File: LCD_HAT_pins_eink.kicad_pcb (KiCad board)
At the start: 4 copper layers, 45.7 x 80.4 mm, 32 parts, among them J1 Qwiic, J2 LCD, J3 PWR_JUMPER, J5 AFC24-S24FIC-00, Q1 Si1308, SW1 SW_Push, SW2 SW_Push, U1 SeeeduinoXIAO

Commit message: FAB Files 1.0
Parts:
- removed J3: PWR_JUMPER, Connector_PinHeader_2.54mm:PinHeader_1x02_P2.54mm_Vertical
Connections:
- J2 pad 2: Net-(J2-Pin_2) -> +3.3V
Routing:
- net Net-(J2-Pin_2): track 8.72 -> 0.00 mm

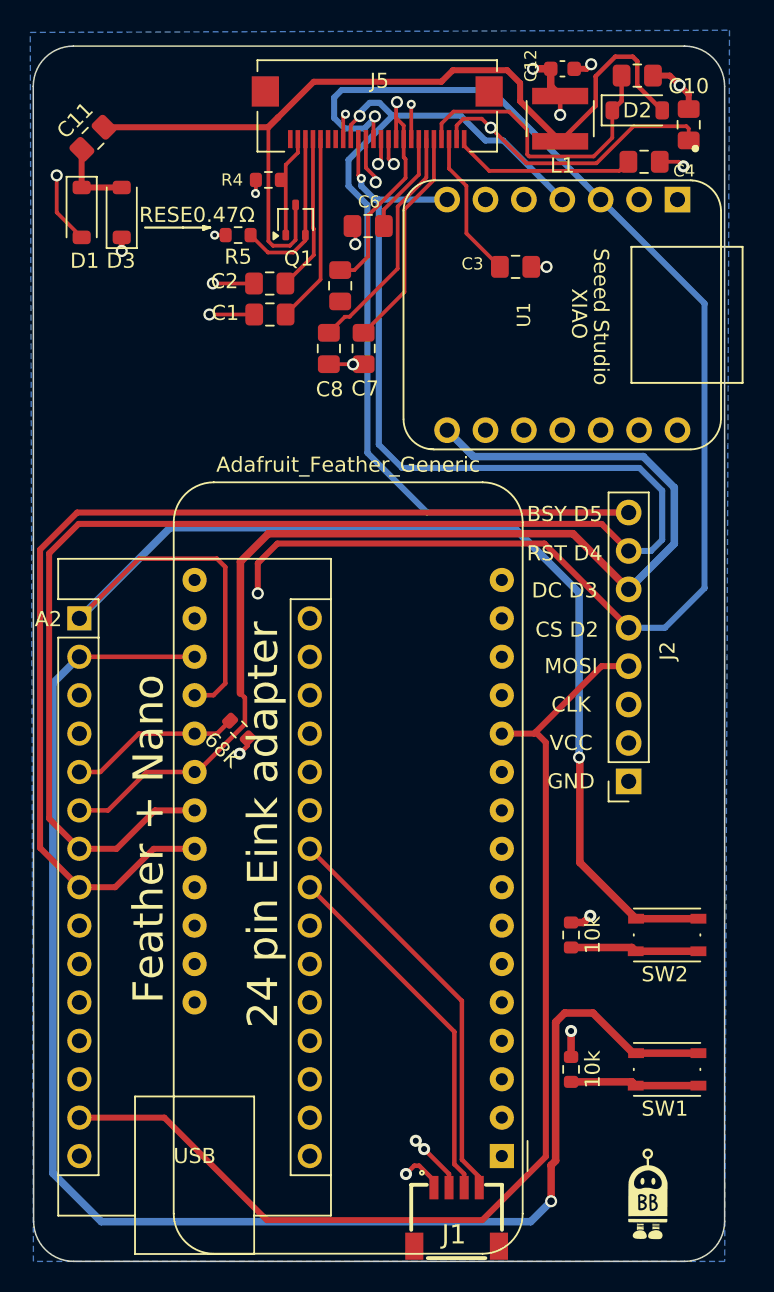
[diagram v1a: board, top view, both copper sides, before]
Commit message: FIX pin not connected to GND in 24 pin FPC
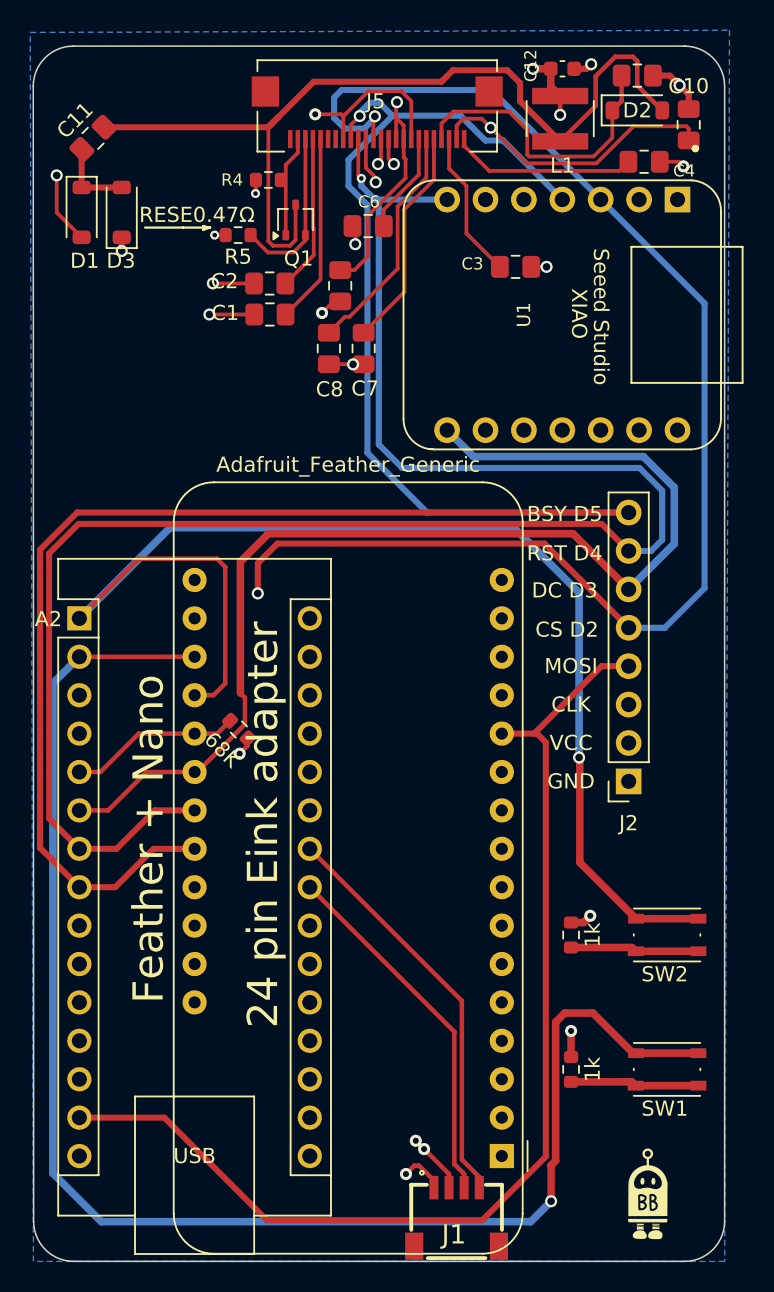
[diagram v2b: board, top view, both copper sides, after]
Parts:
- J5: value AFC24-S24FIC-00 -> CONN_AFC24-S24FIC-00_JUS
- R1, R2: value 10k -> 1k
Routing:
- net GND: track 29.9 -> 38.3 mm
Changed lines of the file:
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@@
 		(sheetname "/")
 		(sheetfile "LCD_HAT_pins_eink.kicad_sch")
-		(attr through_hole exclude_from_bom)
+		(attr through_hole exclude_from_pos_files exclude_from_bom)
 		(fp_line
 			(start -1.4 -3.94)
@@
 			)
 		)
-		(property "Value" "10k"
+		(property "Value" "1k"
 			(at 0 1.43 90)
 			(layer "F.SilkS")
@@
 		(at 134.5 42.954399 180)
 		(property "Reference" "J5"
-			(at -0.15 1.654399 0)
+			(at 0.1 0.304399 0)
 			(layer "F.SilkS")
 			(effects
@@
 			)
 		)
-		(property "Value" "AFC24-S24FIC-00"
-			(at 0.49 4 0)
+		(property "Value" "CONN_AFC24-S24FIC-00_JUS"
+			(at 0.49 4 180)
 			(layer "F.SilkS")
 			(hide yes)
@@
 		)
 		(property "Datasheet" ""
-			(at 0 0 0)
+			(at 0 0 180)
 			(layer "F.Fab")
 			(hide yes)
@@
 		)
 		(property "Description" ""
-			(at 0 0 0)
-			(layer "F.Fab")
-			(hide yes)
-			(effects
-				(font
-					(size 1.27 1.27)
-					(thickness 0.15)
-				)
-			)
-		)
-		(property "LCSC" "C262292"
 			(at 0 0 180)
-			(unlocked yes)
 			(layer "F.Fab")
 			(hide yes)
 			(effects
 				(font
-					(size 1 1)
+					(size 1.27 1.27)
 					(thickness 0.15)
 				)
@@
 		(sheetname "/")
 		(sheetfile "LCD_HAT_pins_eink.kicad_sch")
-		(attr through_hole)
+		(attr smd)
 		(fp_line
 			(start 7.9248 3.022599)
@@
 		)
 		(fp_text user "*"
-			(at 0 0 0)
+			(at 0 0 180)
 			(layer "F.SilkS")
 			(hide yes)
@@
 		)
 		(fp_text user "Copyright 2021 Accelerated Designs. All rights reserved."
-			(at 0 0 0)
+			(at 0 0 180)
 			(layer "Cmts.User")
 			(effects
@@
 		)
 		(fp_text user "*"
-			(at 0 0 0)
+			(at 0 0 180)
 			(layer "F.Fab")
 			(effects
@@
 		(sheetname "/")
 		(sheetfile "LCD_HAT_pins_eink.kicad_sch")
-		(attr through_hole exclude_from_bom)
+		(attr through_hole exclude_from_pos_files exclude_from_bom)
 		(fp_line
 			(start 21.7 -3.81)
@@
 		(sheetname "/")
 		(sheetfile "LCD_HAT_pins_eink.kicad_sch")
-		(attr through_hole)
+		(attr smd)
 		(fp_line
 			(start 1.17475 -2.2225)
@@
 			)
 		)
-		(property "Value" "10k"
+		(property "Value" "1k"
 			(at 0 1.43 90)
 			(layer "F.SilkS")
@@
 			)
 		)
-		(property "LCSC" "C25804"
+		(property "LCSC" "C11702"
 			(at 0 0 90)
 			(unlocked yes)
@@
 		(tags "Through hole socket strip THT 1x08 2.54mm single row")
 		(property "Reference" "J2"
-			(at -2.57 8.63 90)
+			(at 0 -2.77 180)
 			(layer "F.SilkS")
 			(effects
@@
 		)
 		(property "Value" "LCD"
-			(at 0 20.55 0)
+			(at 0 20.55 180)
 			(layer "F.Fab")
 			(effects
@@
 		(sheetname "/")
 		(sheetfile "LCD_HAT_pins_eink.kicad_sch")
-		(attr through_hole)
+		(attr through_hole exclude_from_pos_files exclude_from_bom)
 		(fp_line
 			(start 1.33 1.27)
@@
 		)
 		(fp_text user "${REFERENCE}"
-			(at 0 8.89 90)
+			(at 0 8.89 270)
 			(layer "F.Fab")
 			(effects
@@
 			(pintype "passive")
 		)
-		(pad "2" thru_hole oval
+		(pad "2" thru_hole circle
 			(at 0 2.54 180)
 			(size 1.7 1.7)
@@
 			(pintype "passive")
 		)
-		(pad "3" thru_hole oval
+		(pad "3" thru_hole circle
 			(at 0 5.08 180)
 			(size 1.7 1.7)
@@
 			(pintype "passive")
 		)
-		(pad "4" thru_hole oval
+		(pad "4" thru_hole circle
 			(at 0 7.62 180)
 			(size 1.7 1.7)
@@
 			(pintype "passive")
 		)
-		(pad "5" thru_hole oval
+		(pad "5" thru_hole circle
 			(at 0 10.16 180)
 			(size 1.7 1.7)
@@
 			(pintype "passive")
 		)
-		(pad "6" thru_hole oval
+		(pad "6" thru_hole circle
 			(at 0 12.7 180)
 			(size 1.7 1.7)
@@
 			(pintype "passive")
 		)
-		(pad "7" thru_hole oval
+		(pad "7" thru_hole circle
 			(at 0 15.24 180)
 			(size 1.7 1.7)
@@
 			(pintype "passive")
 		)
-		(pad "8" thru_hole oval
+		(pad "8" thru_hole circle
 			(at 0 17.78 180)
 			(size 1.7 1.7)
@@
 		)
 		(embedded_fonts no)
-		(model "${KICAD6_3DMODEL_DIR}/Connector_PinSocket_2.54mm.3dshapes/PinSocket_1x08_P2.54mm_Vertical.wrl"
+		(model "${KICAD9_3DMODEL_DIR}/Connector_PinSocket_2.54mm.3dshapes/PinSocket_1x08_P2.54mm_Vertical.step"
 			(offset
 				(xyz 0 0 0)
@@
 		(sheetname "/")
 		(sheetfile "LCD_HAT_pins_eink.kicad_sch")
-		(attr smd exclude_from_bom)
+		(attr through_hole exclude_from_pos_files exclude_from_bom)
 		(fp_line
 			(start -6.9 10.5)
@@
 	)
 	(segment
+		(start 130.4 43.51)
+		(end 132.109998 43.51)
+		(width 0.25)
+		(layer "F.Cu")
+		(net 45)
+	)
+	(segment
 		(start 126.475 48.725)
 		(end 126.45 48.75)
@@
 	)
 	(segment
+		(start 136.750001 42.631313)
+		(end 136.102562 41.983874)
+		(width 0.25)
+		(layer "F.Cu")
+		(net 45)
+	)
+	(segment
+		(start 136.750001 45.149999)
+		(end 136.750001 42.631313)
+		(width 0.25)
+		(layer "F.Cu")
+		(net 45)
+	)
+	(segment
+		(start 136.102562 41.983874)
+		(end 133.916126 41.983874)
+		(width 0.25)
+		(layer "F.Cu")
+		(net 45)
+	)
+	(segment
 		(start 132.7875 60.0375)
 		(end 132.8 60.05)
@@
 	)
 	(segment
-		(start 136.750001 45.149999)
-		(end 136.75 42.85)
-		(width 0.25)
-		(layer "F.Cu")
-		(net 45)
-	)
-	(segment
 		(start 147.32 105.855)
 		(end 147.32 104.14)
@@
 	)
 	(segment
+		(start 130.41 43.5)
+		(end 130.4 43.51)
+		(width 0.25)
+		(layer "F.Cu")
+		(net 45)
+	)
+	(segment
+		(start 131.6125 55.8875)
+		(end 130.85 56.65)
+		(width 0.25)
+		(layer "F.Cu")
+		(net 45)
+	)
+	(segment
 		(start 148.35 40.5)
 		(end 148.65 40.2)
@@
 	)
 	(segment
+		(start 133.916126 41.983874)
+		(end 132.4 43.5)
+		(width 0.25)
+		(layer "F.Cu")
+		(net 45)
+	)
+	(segment
 		(start 153.85 40.95)
 		(end 154.5 41.6)
@@
 	)
 	(segment
+		(start 132.109998 43.51)
+		(end 132.249999 43.650001)
+		(width 0.25)
+		(layer "F.Cu")
+		(net 45)
+	)
+	(segment
 		(start 124.475 51.5)
 		(end 123.75 51.5)
@@
 	)
 	(via
-		(at 132.4 43.5)
-		(size 0.6)
-		(drill 0.3)
-		(layers "F.Cu" "B.Cu")
-		(net 45)
-	)
-	(via
 		(at 132.9 60.05)
 		(size 0.8)
@@
 	)
 	(via
-		(at 133.05 52.1)
+		(at 130.85 56.65)
 		(size 0.8)
-		(drill 0.5)
+		(drill 0.4)
 		(layers "F.Cu" "B.Cu")
 		(net 45)
 	)
 	(via
-		(at 136.75 42.85)
-		(size 0.6)
-		(drill 0.3)
+		(at 133.05 52.1)
+		(size 0.8)
+		(drill 0.5)
 		(layers "F.Cu" "B.Cu")
 		(net 45)
@@
 		(layers "F.Cu" "B.Cu")
 		(net 45)
+	)
+	(via
+		(at 130.4 43.51)
+		(size 0.8)
+		(drill 0.4)
+		(layers "F.Cu" "B.Cu")
+		(net 45)
